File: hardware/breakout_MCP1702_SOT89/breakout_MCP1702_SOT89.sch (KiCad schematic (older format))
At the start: 7 parts, among them J1 Conn_01x04, J4 Conn_01x04, U1 MCP1702-MB

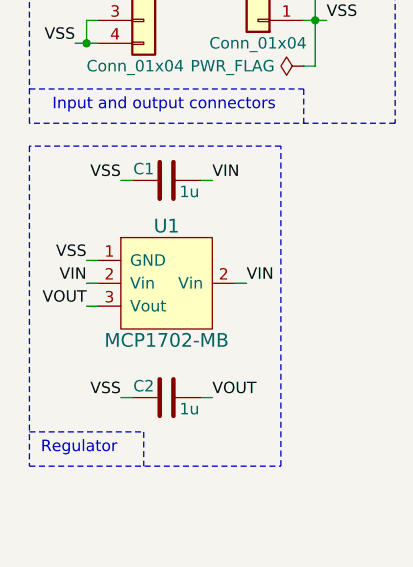
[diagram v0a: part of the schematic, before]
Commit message: updated fonts, different footprint for MCP1702
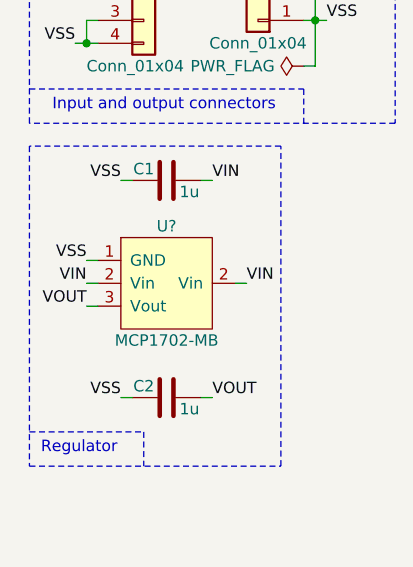
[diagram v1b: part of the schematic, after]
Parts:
- removed U1: MCP1702-MB, SquantorIC:SOT89-NXP, symbol SquantorMicrochip:MCP1702-MB
- added U?: MCP1702-MB, SquantorIC:SOT89-NXP-Viatab, symbol SquantorMicrochip:MCP1702-MB
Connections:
- net VIN: now also U?.2 (Vin)
- net VOUT: now also U?.3 (Vout)
- net VSS: now also U?.1 (GND)
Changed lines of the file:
@@
-$EndComp
-$Comp
-L SquantorMicrochip:MCP1702-MB U1
-U 1 1 5BE4AA1E
-P 1200 2150
-F 0 "U1" H 1200 2400 60  0000 C CNN
-F 1 "MCP1702-MB" H 1200 1900 60  0000 C CNN
-F 2 "SquantorIC:SOT89-NXP" H 1200 2150 60  0001 C CNN
-F 3 "" H 1200 2150 60  0001 C CNN
-	1    1200 2150
-	1    0    0    -1
 $EndComp
 $Comp
@@
 Wire Wire Line
 	1850 1200 1800 1200
+$Comp
+L SquantorMicrochip:MCP1702-MB U?
+U 1 1 5EDF107E
+P 1200 2150
+F 0 "U?" H 1200 2400 50  0000 C CNN
+F 1 "MCP1702-MB" H 1200 1900 50  0000 C CNN
+F 2 "SquantorIC:SOT89-NXP-Viatab" H 1200 2150 60  0001 C CNN
+F 3 "" H 1200 2150 60  0001 C CNN
+	1    1200 2150
+	1    0    0    -1
+$EndComp
 $EndSCHEMATC

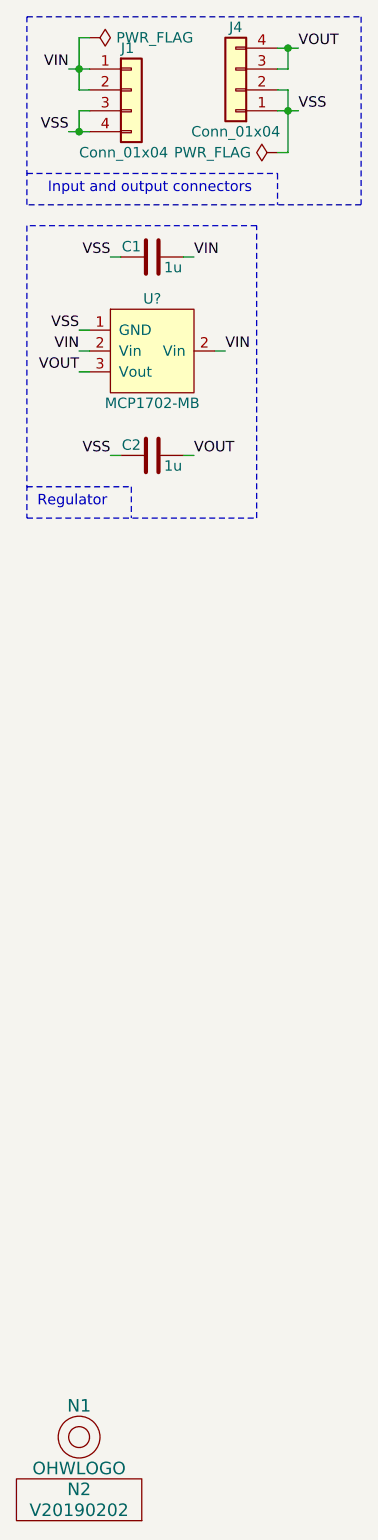
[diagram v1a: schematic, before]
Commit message: minor silk movements
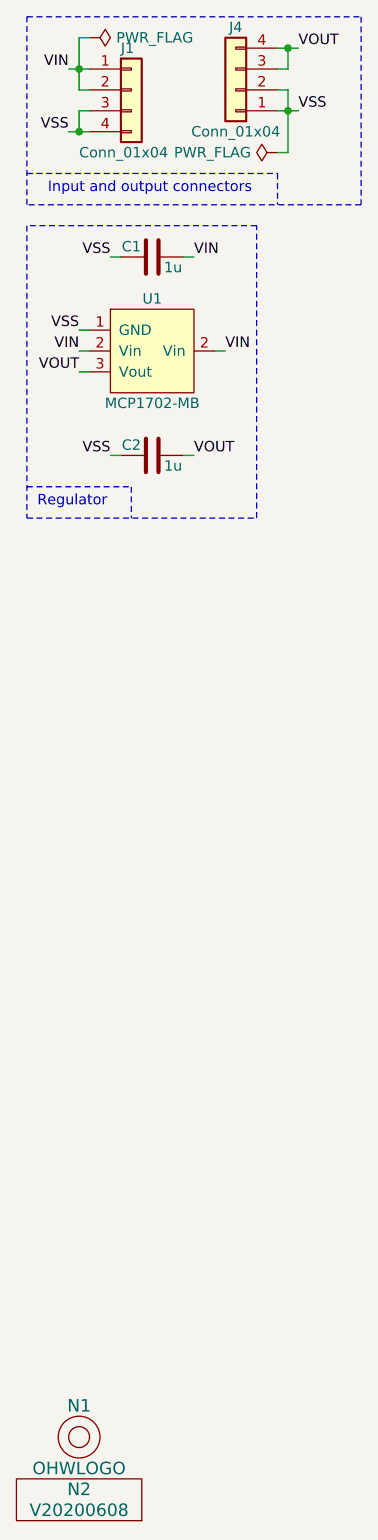
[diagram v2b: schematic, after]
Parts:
- N2: value V20190202 -> V20200608
- gave numbers to parts that had none: 1
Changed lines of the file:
@@
 P 850 7700
 F 0 "N2" H 850 7800 60  0000 C CNN
-F 1 "V20190202" H 850 7700 60  0000 C CNN
+F 1 "V20200608" H 850 7700 60  0000 C CNN
 F 2 "SquantorLabels:Label_Generic" H 850 7700 60  0001 C CNN
 F 3 "" H 850 7700 60  0001 C CNN
@@
 	1850 1200 1800 1200
 $Comp
-L SquantorMicrochip:MCP1702-MB U?
+L SquantorMicrochip:MCP1702-MB U1
 U 1 1 5EDF107E
 P 1200 2150
-F 0 "U?" H 1200 2400 50  0000 C CNN
+F 0 "U1" H 1200 2400 50  0000 C CNN
 F 1 "MCP1702-MB" H 1200 1900 50  0000 C CNN
 F 2 "SquantorIC:SOT89-NXP-Viatab" H 1200 2150 60  0001 C CNN
